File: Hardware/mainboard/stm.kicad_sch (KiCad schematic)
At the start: 38 parts, among them SW1 ON-BOARD, SW2 BOT, SW3 BOOT, U3 STM32F091RCTx, Y1 Crystal_GND24

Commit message: pushing for the evening
didnt add much, just moved things around and fixed footprints
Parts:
- added J10, J5, J8: B4B-EH-A, 1x04_jst_connector:1x04_jst, symbol 1x04_jst:B4B-EH-A
- SW1: footprint Button_Switch_SMD:SW_SPST_CK_RS282G05A3 -> Button_Switch_SMD:SW_Tactile_SPST_NO_Straight_CK_PTS636Sx25SMTRLFS
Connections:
- net EOT_RUN_STAT: now also J10.3
- net GND: now also J5.4, J8.4
- net PC13: now also J5.1, J8.1
- net PC14: now also J5.2, J8.2
- net PC15: now also J10.4, J5.3, J8.3
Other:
- note added: "BOT"
- note added: "I'll use 3 different colors for these LEDs. theyll sit at the end of the track (EOT) and the beginning of the track (BOT)."
- note added: "ON"
- note added: "Status LEDs"
- moved on the sheet: D10, D11, D12, D13, D4, D5, D6, D7, D8, D9, R10, R11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

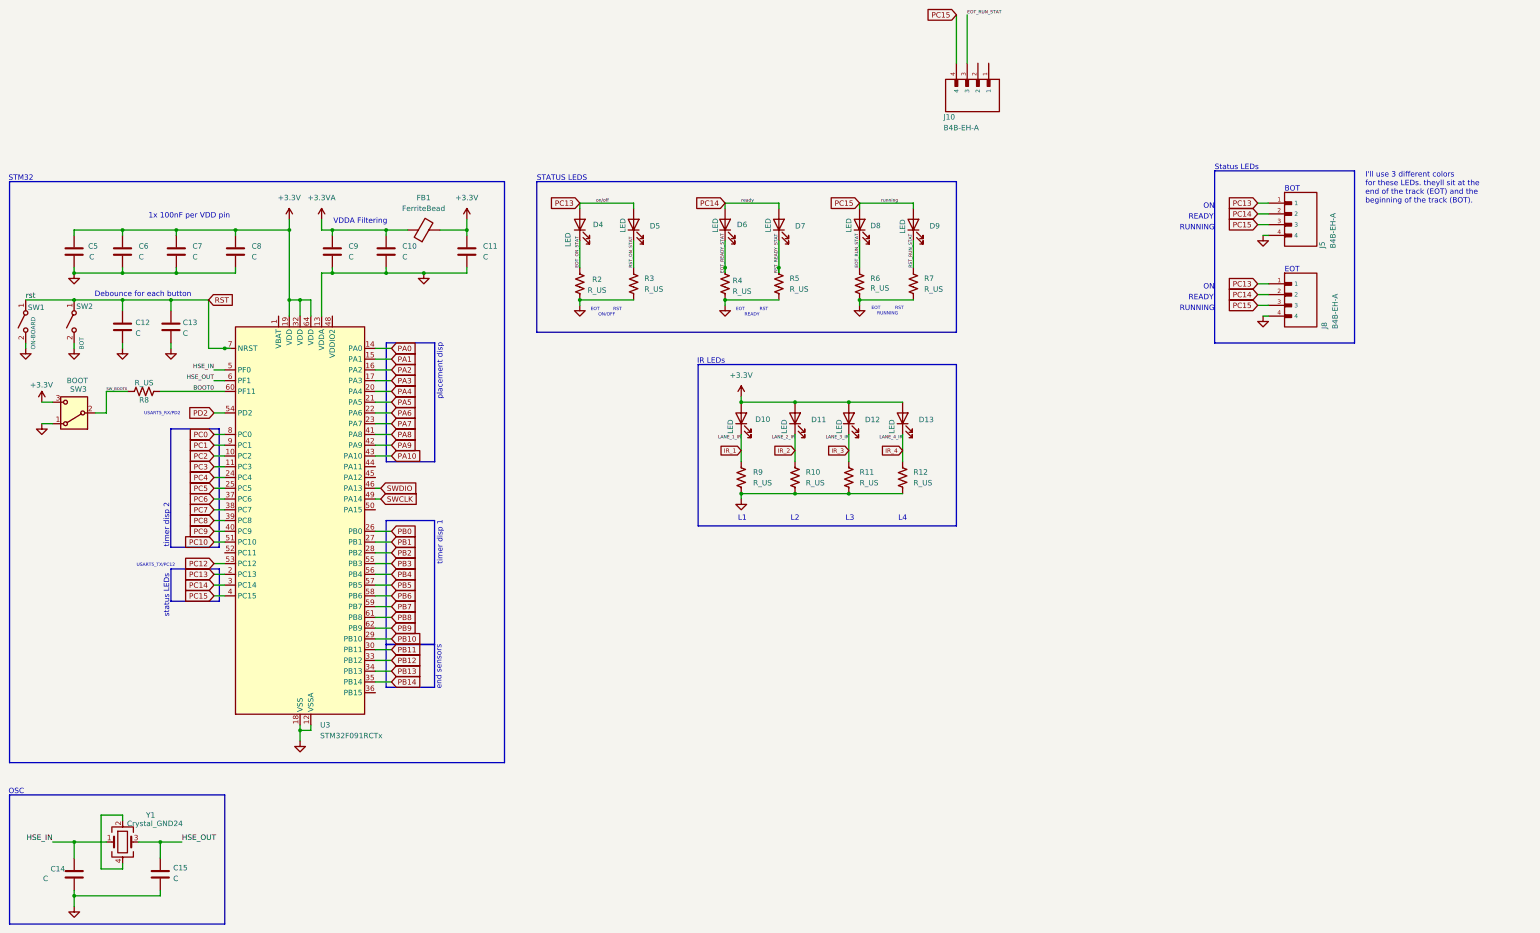
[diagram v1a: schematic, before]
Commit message: Lowkey forgot the start switch so i added that
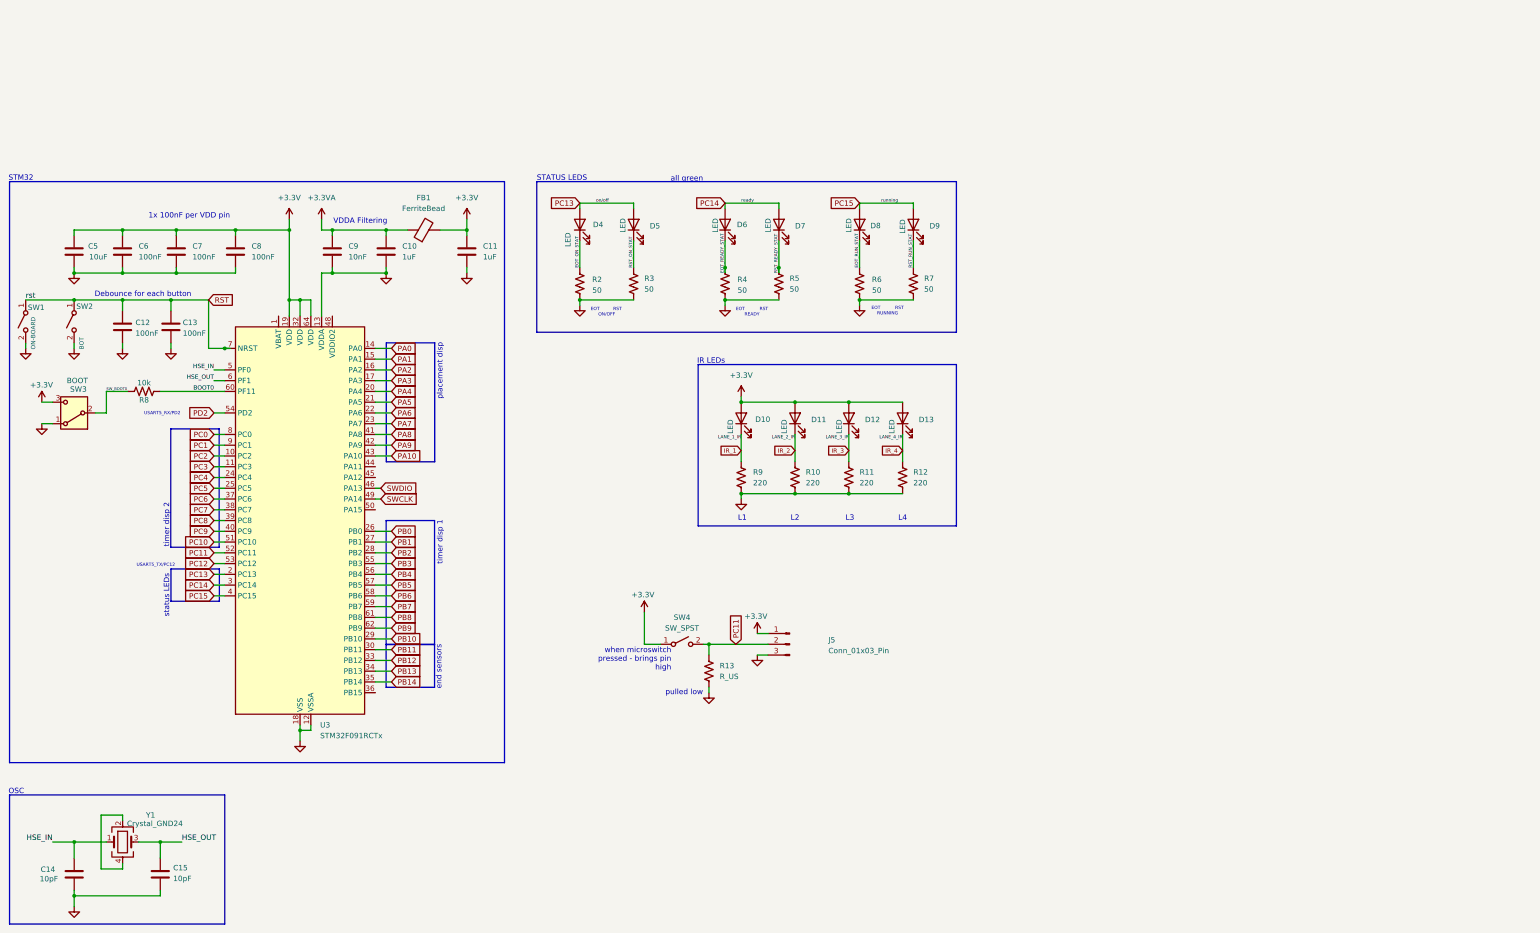
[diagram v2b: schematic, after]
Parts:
- removed J10, J5, J8: B4B-EH-A, 1x04_jst_connector:1x04_jst, symbol 1x04_jst:B4B-EH-A
- added J5: Conn_01x03_Pin, symbol Connector:Conn_01x03_Pin
- added R13: R_US, symbol Device:R_US
- added SW4: SW_SPST, symbol Switch:SW_SPST
- C10, C11: value C -> 1uF
- C12, C13, C6, C7, C8: value C -> 100nF
- C14, C15: value C -> 10pF
- C5: value C -> 10uF
- C9: value C -> 10nF
- R10, R11, R12, R9: value R_US -> 220
- R2, R3, R4, R5, R6, R7: value R_US -> 50
- R8: value R_US -> 10k
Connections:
- net +3.3V: now also J5.1 (Pin_1), SW4.1 (A)
- net GND: now also J5.3 (Pin_3), R13.2
- net PC11: now reaches U3.52 (PC11)
- net PC11: now also J5.2 (Pin_2), R13.1, SW4.2 (B)
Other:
- note added: "all green"
- note added: "pulled low"
- note added: "when microswitch pressed - brings pin high"
- note removed: "BOT"
- note removed: "I'll use 3 different colors for these LEDs. theyll sit at the end of the track (EOT) and the beginning of the track (BOT)."
- note removed: "ON"
- note removed: "Status LEDs"

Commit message: layout
worked on the layput but im actively falling asleep while working on it so im going to call it a day
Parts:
- SW3: footprint Connector_PinHeader_1.00mm:PinHeader_1x03_P1.00mm_Vertical -> Connector_PinHeader_2.54mm:PinHeader_1x03_P2.54mm_Vertical
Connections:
- no-connect marks 0 -> 5
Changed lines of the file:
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@@
 		(color 0 0 0 0)
 	)
+	(no_connect
+		(at 93.98 49.53)
+	)
+	(no_connect
+		(at 104.14 95.25)
+	)
+	(no_connect
+		(at 104.14 138.43)
+	)
+	(no_connect
+		(at 104.14 87.63)
+	)
+	(no_connect
+		(at 104.14 85.09)
+	)
 	(wire
 		(pts
@@
 			)
 		)
-		(property "Footprint" "Connector_PinHeader_1.00mm:PinHeader_1x03_P1.00mm_Vertical"
+		(property "Footprint" "Connector_PinHeader_2.54mm:PinHeader_1x03_P2.54mm_Vertical"
 			(at 33.02 72.39 0)
 			(effects
